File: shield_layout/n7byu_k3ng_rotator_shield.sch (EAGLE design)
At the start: 26 parts, among them J1 ARDUINO_R3_SHIELD

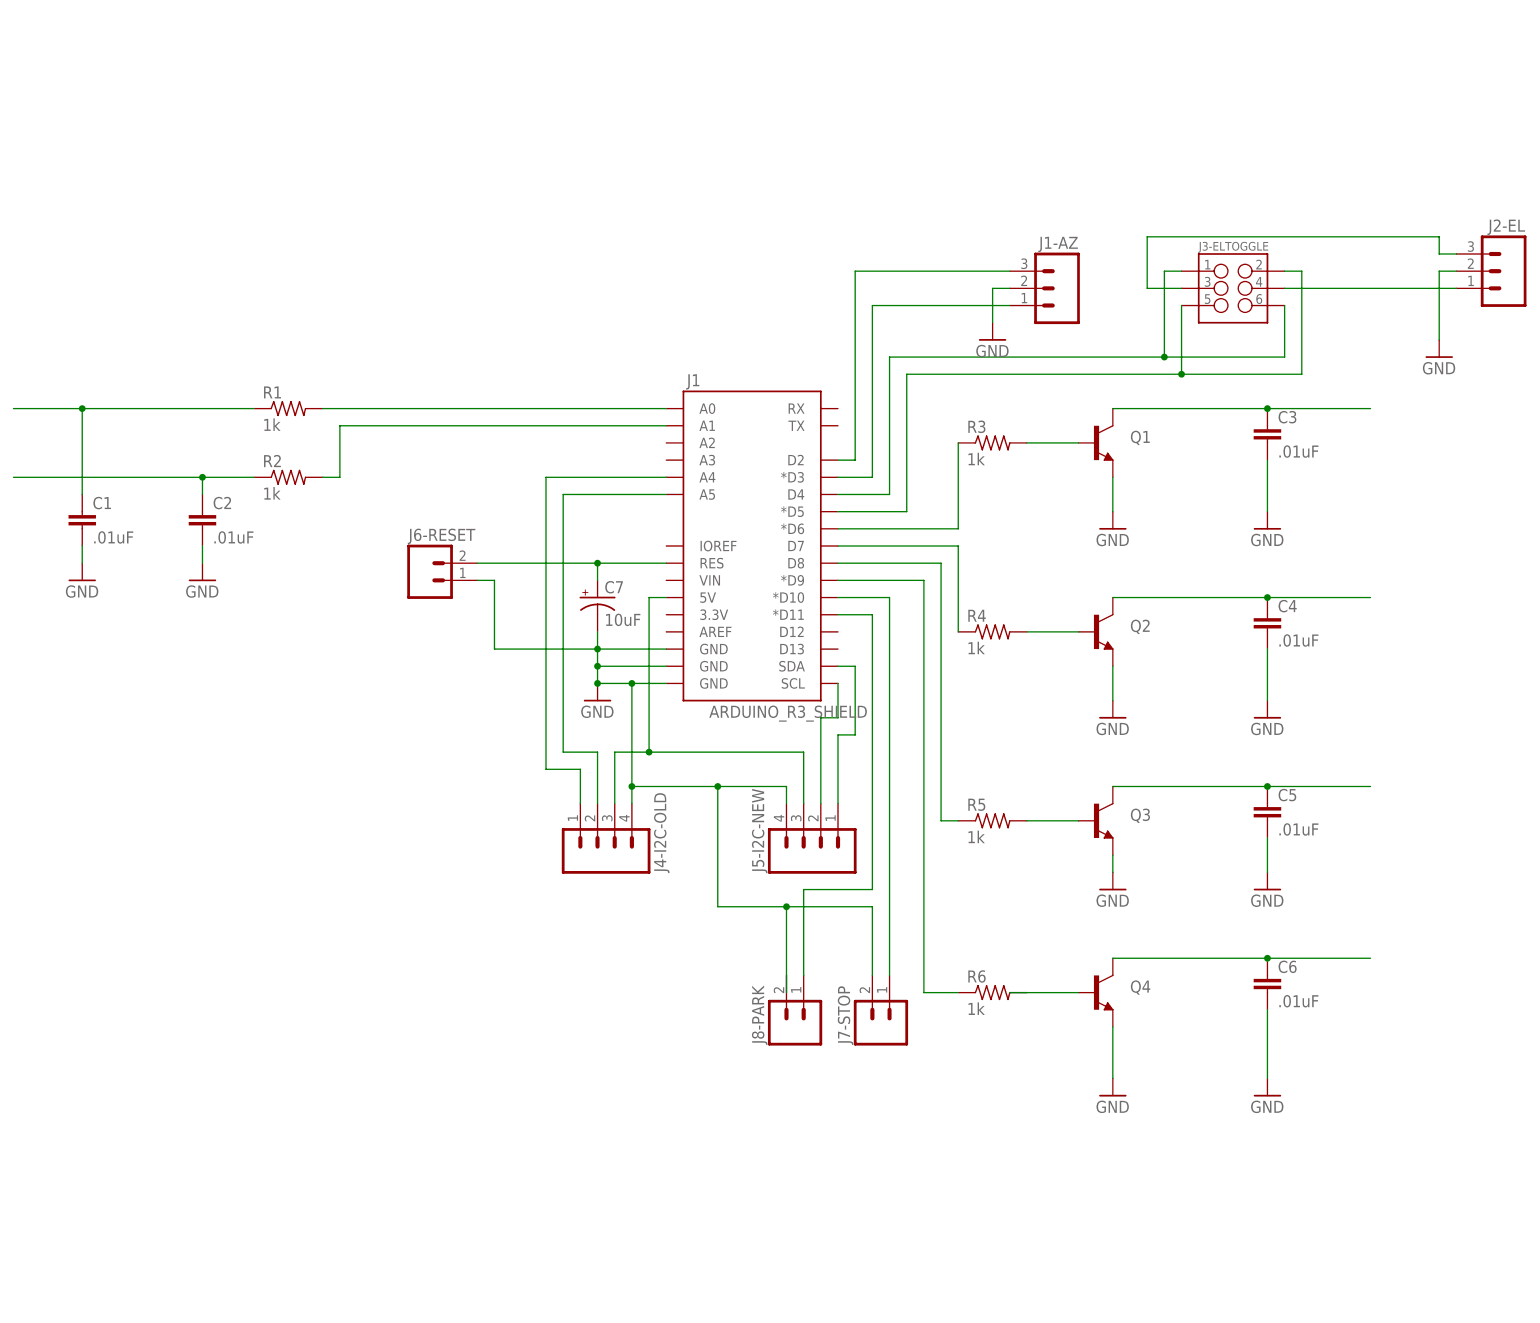
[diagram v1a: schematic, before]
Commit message: converting to 2-row headers to save on space
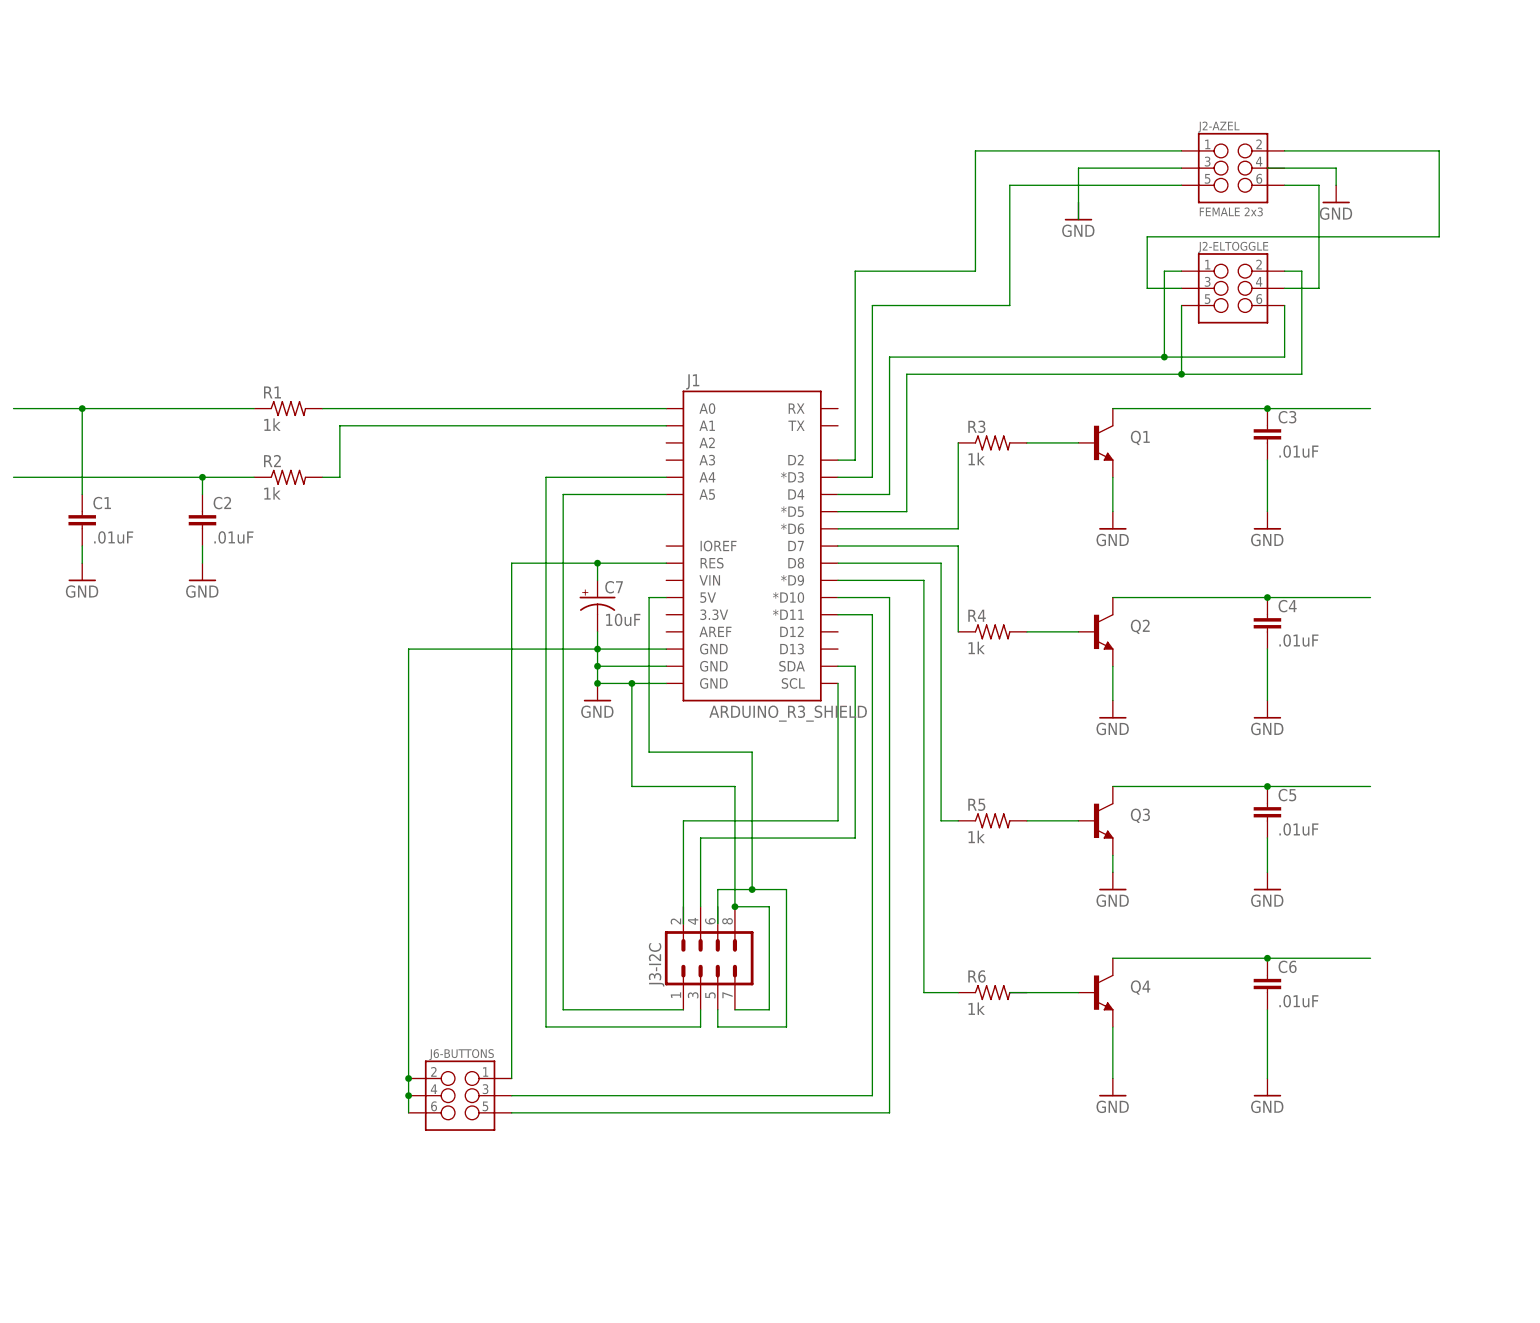
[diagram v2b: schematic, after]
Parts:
- removed J1-AZ, J2-EL: (no value), SparkFun-Connectors:M03LONGPADS
- removed J4-I2C-OLD, J5-I2C-NEW: (no value), SparkFun-Connectors:M04LONGPADS
- removed J6-RESET, J7-STOP, J8-PARK: (no value), SparkFun-Connectors:M02PTH3
- added J2-AZEL: FEMALE 2x3, SparkFun-Connectors:M03X2FEMALE
- added J3-I2C: (no value), SparkFun-Connectors:M04X2
- added J6-BUTTONS: (no value), SparkFun-Connectors:M03X22X3_SILK_MALE_PTH
- renumbered J3-ELTOGGLE to J2-ELTOGGLE
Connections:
- removed net N$18: J1-AZ.1, J1.*D3
- removed net N$20: J1-AZ.3, J1.D2
- removed net N$30: J1.5V, J4-I2C-OLD.3, J5-I2C-NEW.3
- new net CCW-BUTTON: J1.*D3, J2-AZEL.5
- new net CW-BUTTON: J1.D2, J2-AZEL.1
- new net N$31: J1.*D11, J6-BUTTONS.3
- new net N$32: J1.SCL
- net GND: now also J3-I2C.7, J3-I2C.8, J6-BUTTONS.2, J6-BUTTONS.4, J6-BUTTONS.6; no longer J1-AZ.2, J2-EL.2, J4-I2C-OLD.4, J5-I2C-NEW.4, J6-RESET.1, J7-STOP.2
- net N$13: now also J6-BUTTONS.1; no longer J6-RESET.2
- net N$14: now also J2-AZEL.6; no longer J2-EL.1
- net N$21: now also J2-AZEL.2; no longer J2-EL.3
- net N$22: now also J2-AZEL.3; no longer J1.A4, J4-I2C-OLD.1
- net N$25: now also J3-I2C.1; no longer J4-I2C-OLD.2
- net N$26: now also J1.5V, J3-I2C.5; no longer J1.SCL, J5-I2C-NEW.2
- net N$27: now also J1.A4, J3-I2C.3; no longer J1.SDA, J5-I2C-NEW.1
- net N$28: now also J6-BUTTONS.5; no longer J7-STOP.1
- net N$29: now also J1.SDA, J3-I2C.4; no longer J1.*D11, J8-PARK.1

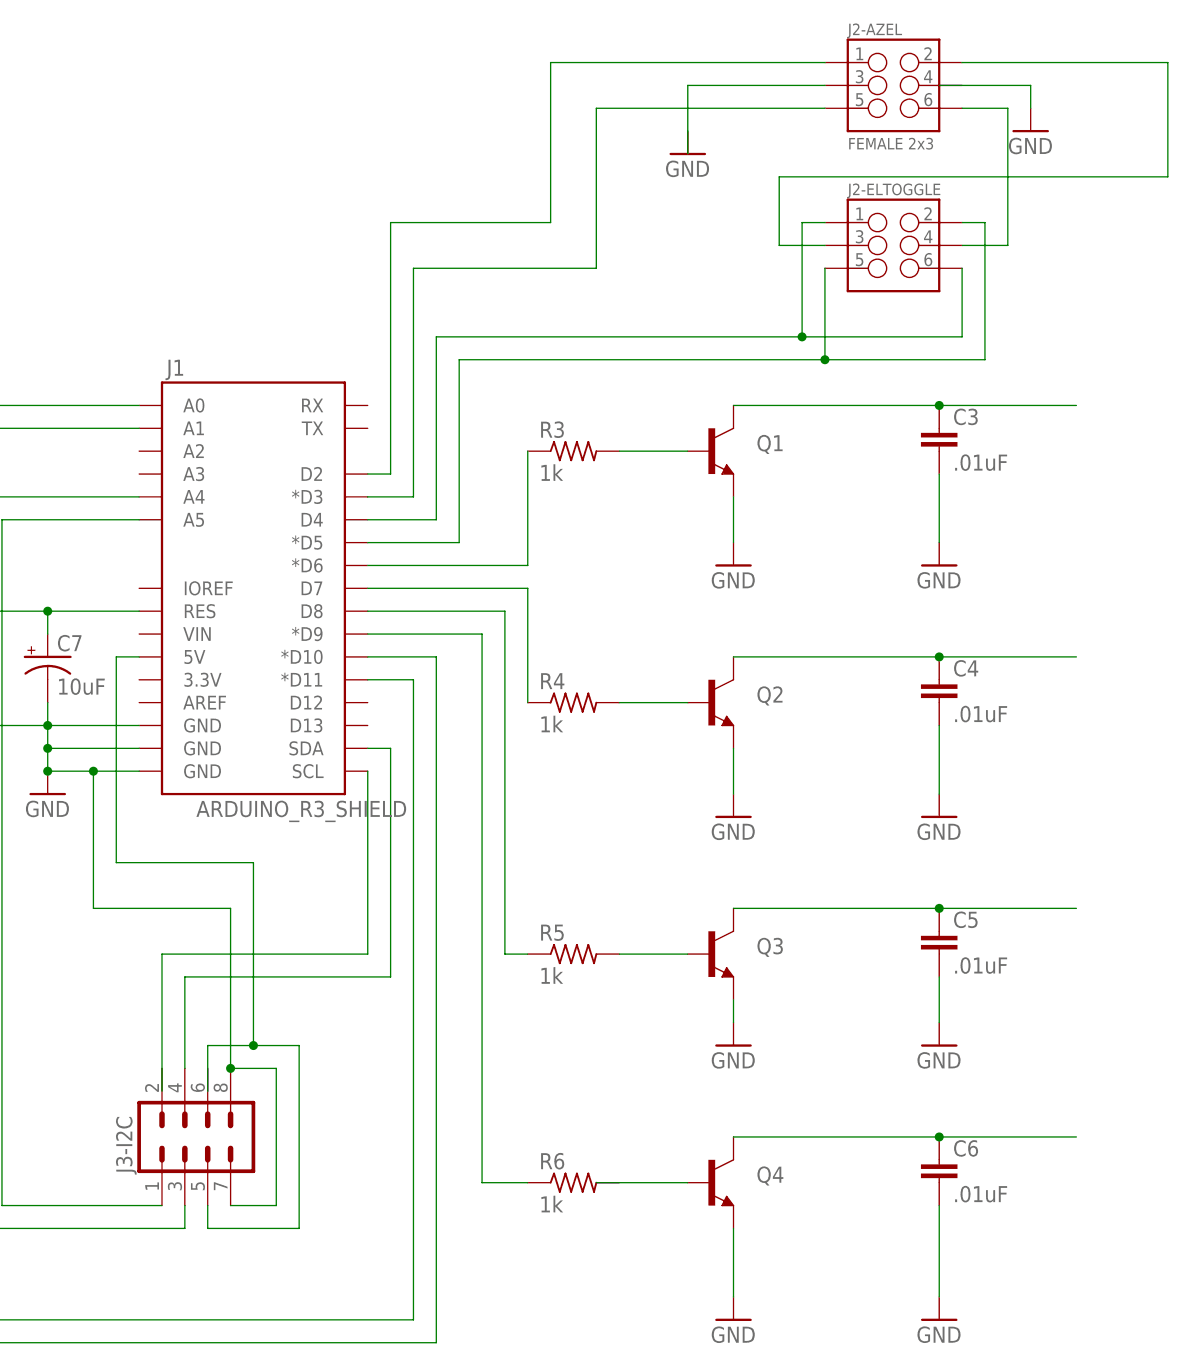
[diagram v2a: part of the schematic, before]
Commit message: begining board layout, using 2 layers; would still like to get down to a single layer if possible
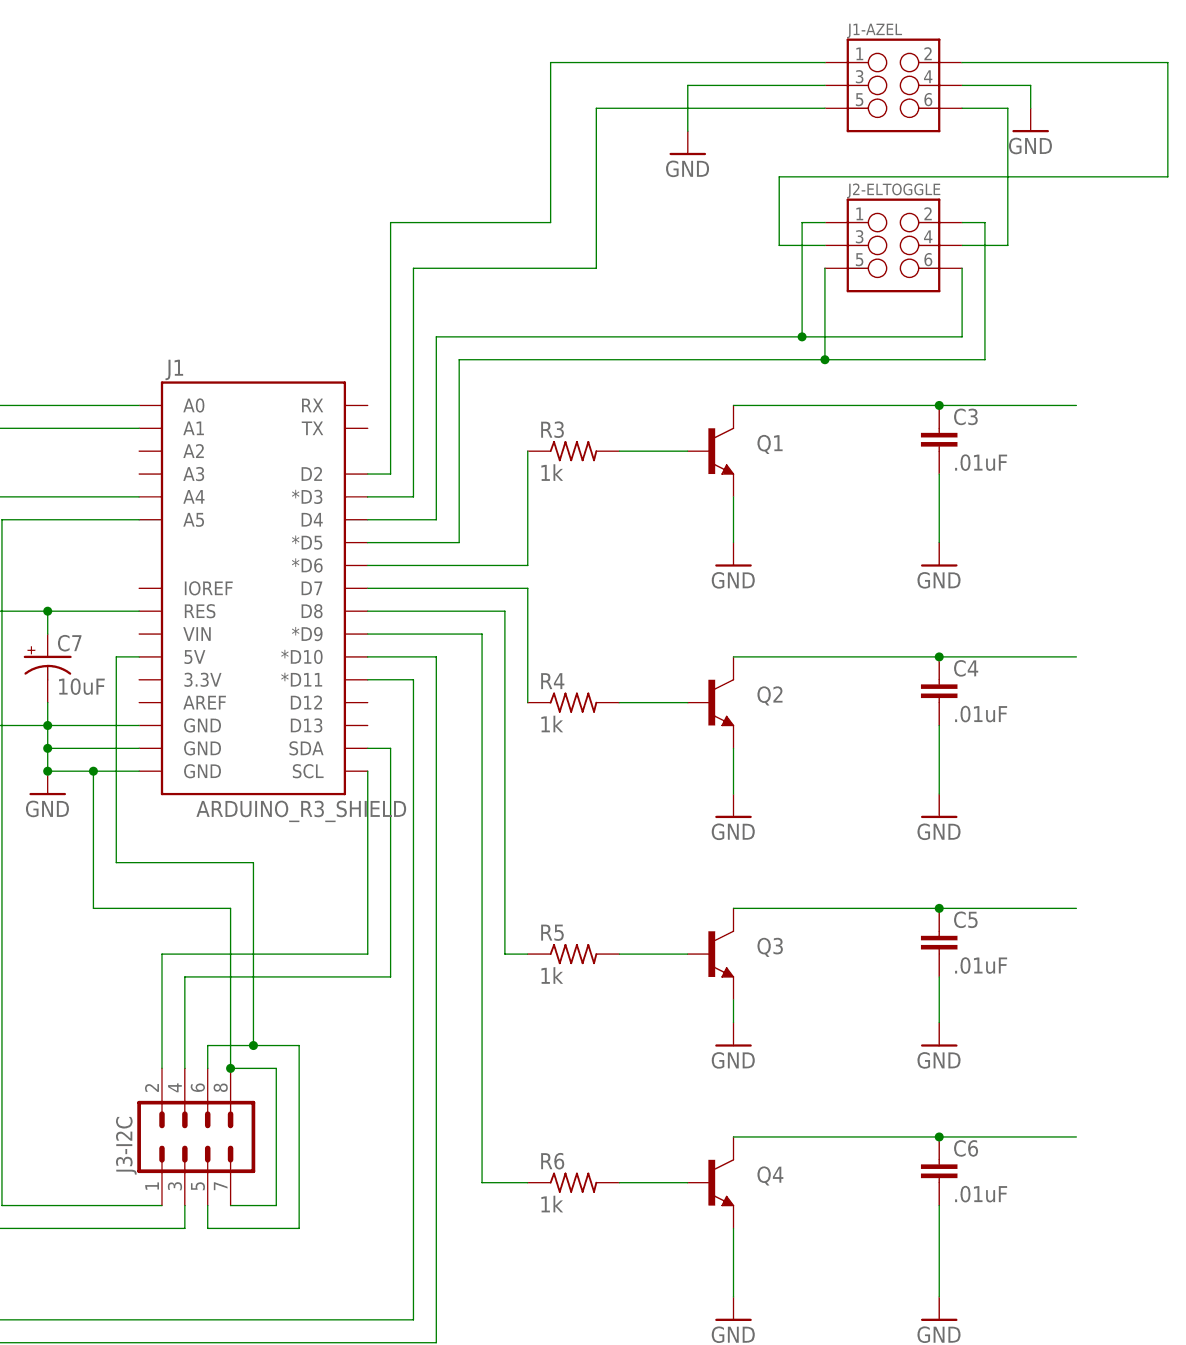
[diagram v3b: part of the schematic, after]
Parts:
- removed J2-AZEL: FEMALE 2x3, SparkFun-Connectors:M03X2FEMALE
- added J1-AZEL: (no value), SparkFun-Connectors:M03X22X3_SILK_MALE_PTH
- C7: device SparkFun-Capacitors:100UF-63V-20%(ELECT) -> SparkFun-Capacitors:CAP_POLPTH1
- J2-ELTOGGLE: device SparkFun-Connectors:M03X2FEMALE -> SparkFun-Connectors:M03X22X3_SILK_MALE_PTH
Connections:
- removed net N$22: J2-AZEL.3
- net CCW-BUTTON: now also J1-AZEL.5; no longer J2-AZEL.5
- net CW-BUTTON: now also J1-AZEL.1; no longer J2-AZEL.1
- net GND: now also J1-AZEL.3, J1-AZEL.4
- net N$14: now also J1-AZEL.6; no longer J2-AZEL.6
- net N$21: now also J1-AZEL.2; no longer J2-AZEL.2
- net N$26: now also J3-I2C.6
- net N$32: now also J3-I2C.2
- net N$8: now also R6.2
